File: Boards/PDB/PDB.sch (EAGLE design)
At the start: 44 parts, among them Q1 NMOS, Q2 IRFML8244, Q3 PMOS, Q4 PMOS, Q5 PMOS

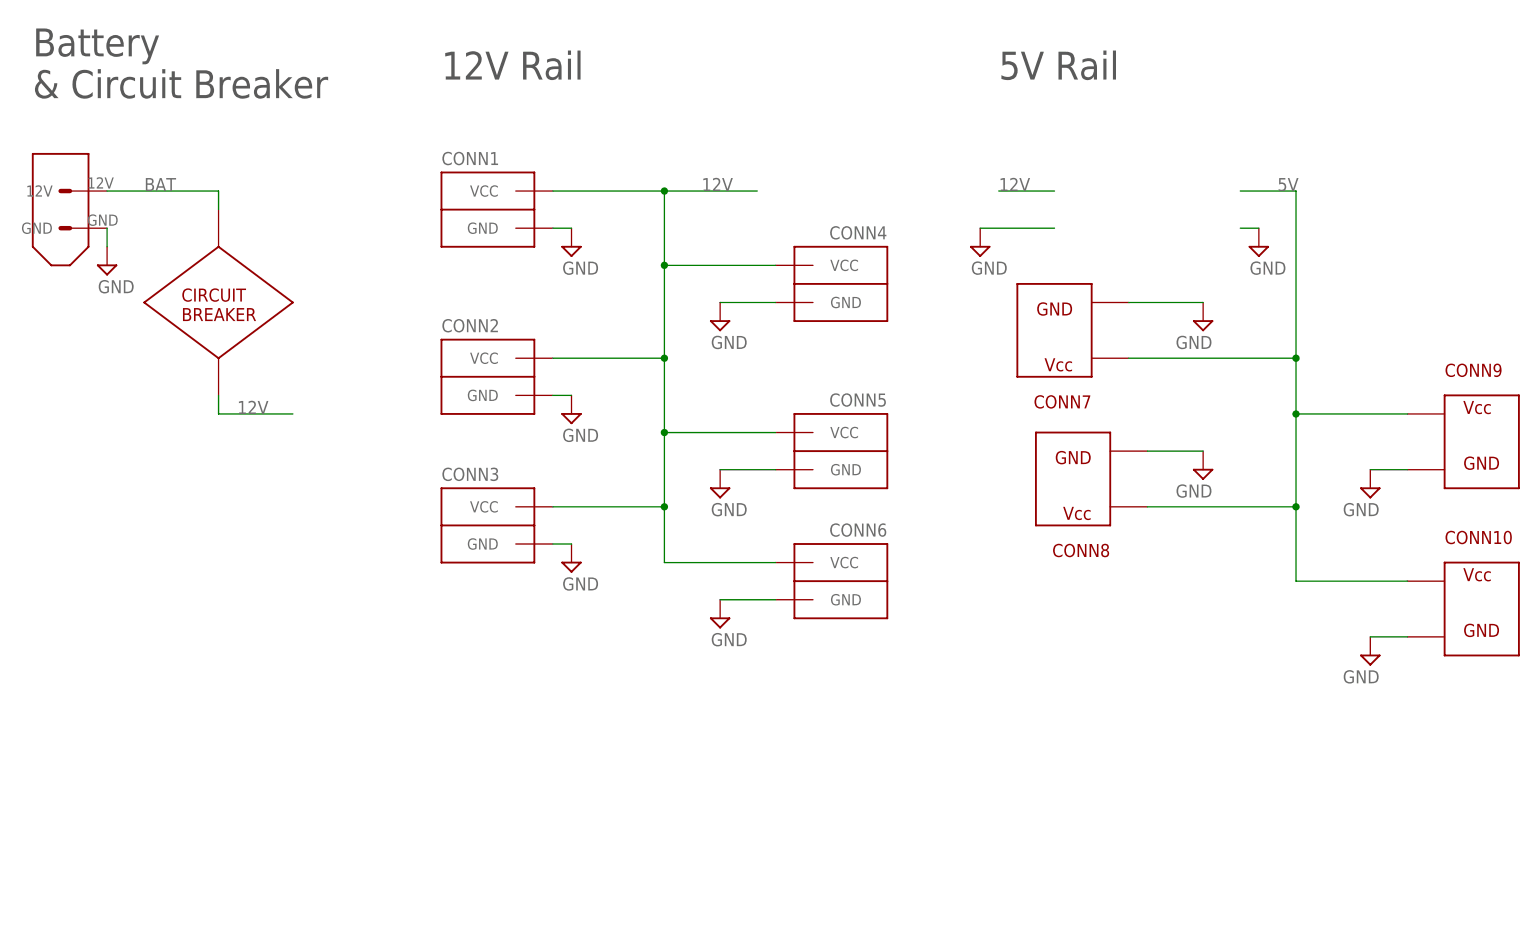
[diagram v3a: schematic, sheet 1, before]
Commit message: Added back 5V buck and added caps. DRC clean
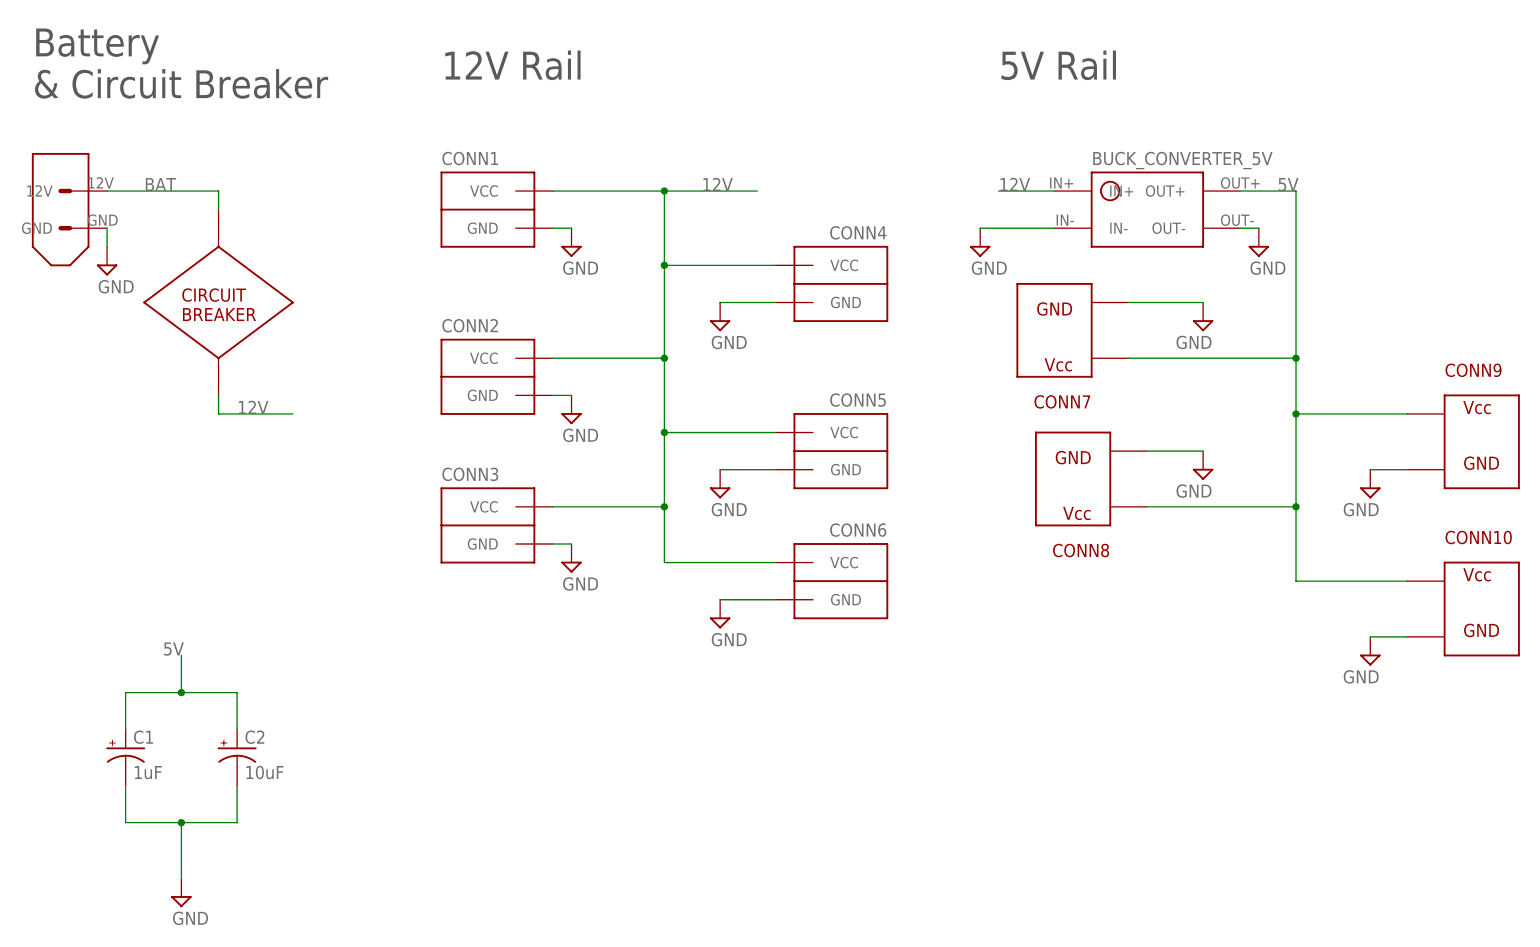
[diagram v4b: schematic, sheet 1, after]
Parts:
- added C1: 1uF, rcl:CPOL-USE5-5
- added C2: 10uF, rcl:CPOL-USE5-5
- added U$1: BUCK_CONVERTER_5V, pie:BUCK_CONVERTER_5V
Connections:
- net 12V: now also U$1.IN+
- net 5V: now also C1.+, C2.+, U$1.OUT+
- net GND: now also C1.-, C2.-, U$1.IN-, U$1.OUT-
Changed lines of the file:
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@@
 <?xml version="1.0" encoding="utf-8"?>
 <!DOCTYPE eagle SYSTEM "eagle.dtd">
-<eagle version="8.0.0">
+<eagle version="8.3.2">
 <drawing>
 <settings>
 <setting alwaysvectorfont="no"/>
+<setting keepoldvectorfont="yes"/>
 <setting verticaltext="up"/>
 </settings>
@@
 <layer number="2" name="Route2" color="1" fill="3" visible="no" active="no"/>
 <layer number="3" name="Route3" color="4" fill="3" visible="no" active="no"/>
+<layer number="4" name="Route4" color="1" fill="4" visible="no" active="no"/>
+<layer number="5" name="Route5" color="4" fill="4" visible="no" active="no"/>
+<layer number="6" name="Route6" color="1" fill="8" visible="no" active="no"/>
+<layer number="7" name="Route7" color="4" fill="8" visible="no" active="no"/>
+<layer number="8" name="Route8" color="1" fill="2" visible="no" active="no"/>
+<layer number="9" name="Route9" color="4" fill="2" visible="no" active="no"/>
+<layer number="10" name="Route10" color="1" fill="7" visible="no" active="no"/>
+<layer number="11" name="Route11" color="4" fill="7" visible="no" active="no"/>
+<layer number="12" name="Route12" color="1" fill="5" visible="no" active="no"/>
+<layer number="13" name="Route13" color="4" fill="5" visible="no" active="no"/>
 <layer number="14" name="Route14" color="1" fill="6" visible="no" active="no"/>
 <layer number="15" name="Route15" color="4" fill="6" visible="no" active="no"/>
@@
 <part name="FRAME1" library="pie" deviceset="FRAME_SCHEMATIC" device="">
 <attribute name="AUTHOR" value="Mohammed H., Sharabesh R., Tobin H."/>
-<attribute name="REVISION" value="10A"/>
+<attribute name="REVISION" value="10C"/>
 </part>
 <part name="XT60" library="pie" deviceset="XT60CONNECTOR" device=""/>
@@
 <part name="FRAME2" library="pie" deviceset="FRAME_SCHEMATIC" device="">
 <attribute name="AUTHOR" value="Casey D, Douglas H, Mohammed H, Tobin H"/>
-<attribute name="REVISION" value="9C"/>
+<attribute name="REVISION" value="10C"/>
 </part>
 <part name="JP1" library="pie" deviceset="XH_CONNECTOR_4POS" device="" value="XH_CONN"/>
@@
 <part name="CONN9" library="pie" deviceset="ATX" device=""/>
 <part name="CONN10" library="pie" deviceset="ATX" device=""/>
+<part name="C1" library="rcl" library_urn="urn:adsk.eagle:library:334" deviceset="CPOL-US" device="E5-5" package3d_urn="urn:adsk.eagle:package:23367/1" value="1uF"/>
+<part name="C2" library="rcl" library_urn="urn:adsk.eagle:library:334" deviceset="CPOL-US" device="E5-5" package3d_urn="urn:adsk.eagle:package:23367/1" value="10uF"/>
+<part name="SUPPLY28" library="pie" deviceset="GND" device=""/>
+<part name="U$1" library="pie" deviceset="BUCK_CONVERTER_5V" device=""/>
 </parts>
 <sheets>
@@
 <instance part="CONN9" gate="CONN$1" x="208.28" y="114.3"/>
 <instance part="CONN10" gate="CONN$1" x="208.28" y="91.44"/>
+<instance part="C1" gate="G$1" x="22.86" y="71.12"/>
+<instance part="C2" gate="G$1" x="38.1" y="71.12"/>
+<instance part="SUPPLY28" gate="GND" x="30.48" y="50.8"/>
+<instance part="U$1" gate="G$1" x="162.56" y="144.78"/>
 </instances>
 <busses>
@@
 <wire x1="149.86" y1="147.32" x2="142.24" y2="147.32" width="0.1524" layer="91"/>
 <label x="142.24" y="147.32" size="1.778" layer="95"/>
+<pinref part="U$1" gate="G$1" pin="IN+"/>
 </segment>
 <segment>
@@
 <wire x1="149.86" y1="142.24" x2="139.7" y2="142.24" width="0.1524" layer="91"/>
 <pinref part="SUPPLY12" gate="GND" pin="GND"/>
+<pinref part="U$1" gate="G$1" pin="IN-"/>
 </segment>
 <segment>
 <pinref part="SUPPLY13" gate="GND" pin="GND"/>
 <wire x1="175.26" y1="142.24" x2="177.8" y2="142.24" width="0.1524" layer="91"/>
+<pinref part="U$1" gate="G$1" pin="OUT-"/>
 </segment>
 <segment>
@@
 <wire x1="198.12" y1="86.36" x2="193.04" y2="86.36" width="0.1524" layer="91"/>
 <pinref part="CONN10" gate="CONN$1" pin="P$2"/>
+</segment>
+<segment>
+<pinref part="C1" gate="G$1" pin="-"/>
+<wire x1="22.86" y1="66.04" x2="22.86" y2="60.96" width="0.1524" layer="91"/>
+<pinref part="C2" gate="G$1" pin="-"/>
+<wire x1="22.86" y1="60.96" x2="30.48" y2="60.96" width="0.1524" layer="91"/>
+<wire x1="30.48" y1="60.96" x2="38.1" y2="60.96" width="0.1524" layer="91"/>
+<wire x1="38.1" y1="60.96" x2="38.1" y2="66.04" width="0.1524" layer="91"/>
+<wire x1="30.48" y1="60.96" x2="30.48" y2="53.34" width="0.1524" layer="91"/>
+<junction x="30.48" y="60.96"/>
+<pinref part="SUPPLY28" gate="GND" pin="GND"/>
 </segment>
 </net>
@@
 <junction x="182.88" y="104.14"/>
 <wire x1="198.12" y1="93.98" x2="182.88" y2="93.98" width="0.1524" layer="91"/>
+<pinref part="U$1" gate="G$1" pin="OUT+"/>
+</segment>
+<segment>
+<pinref part="C1" gate="G$1" pin="+"/>
+<wire x1="22.86" y1="73.66" x2="22.86" y2="78.74" width="0.1524" layer="91"/>
+<pinref part="C2" gate="G$1" pin="+"/>
+<wire x1="22.86" y1="78.74" x2="30.48" y2="78.74" width="0.1524" layer="91"/>
+<wire x1="30.48" y1="78.74" x2="38.1" y2="78.74" width="0.1524" layer="91"/>
+<wire x1="38.1" y1="78.74" x2="38.1" y2="73.66" width="0.1524" layer="91"/>
+<wire x1="30.48" y1="78.74" x2="30.48" y2="83.82" width="0.1524" layer="91"/>
+<junction x="30.48" y="78.74"/>
+<label x="27.94" y="83.82" size="1.778" layer="95" font="vector"/>
 </segment>
 </net>
@@
 which will not be processed correctly with this version.
 </note>
+<note version="8.2" severity="warning">
+Since Version 8.2, EAGLE supports online libraries. The ids
+of those online libraries will not be understood (or retained)
+with this version.
+</note>
+<note version="8.3" severity="warning">
+Since Version 8.3, EAGLE supports URNs for individual library
+assets (packages, symbols, and devices). The URNs of those assets
+will not be understood (or retained) with this version.
+</note>
+<note version="8.3" severity="warning">
+Since Version 8.3, EAGLE supports the association of 3D packages
+with devices in libraries, schematics, and board files. Those 3D
+packages will not be understood (or retained) with this version.
+</note>
 </compatibility>
